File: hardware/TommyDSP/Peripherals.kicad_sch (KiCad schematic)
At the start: 36 parts, among them J501 USB_C_Receptacle_USB2.0_16P, J502 PJ-307, J503 XH-2.50mm Horizontal, J504 PJ-307, J505 Conn_01x06_Pin, J506 PJ-307, J507 XH-2.50mm Horizontal, J508 Conn_01x06_Pin, J509 Conn_01x03_Pin, J510 PJ-307, J511 Micro_SD_Card_Det1, SW501 RotaryEncoder_Switch_MP

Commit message: hardware: finalize PCB design
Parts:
- removed J502, J504, J506, J510: PJ-307, Project:Jack_3.5mm_CUI_SJ1-3525N_Horizontal, symbol Connector_Audio:AudioJack3_Ground_SwitchTR
- added C509: 100n, Capacitor_SMD:C_0603_1608Metric, symbol Device:C
- added G501: qwiic_Logo, SparkFun-Qwiic:qwiic_5.5mm, symbol SparkFun-Qwiic:qwiic_Logo
- added J502, J504, J506, J510: AudioJack3_SwitchTR, Project:Jack_3.5mm_CUI_SJ1-3525N_Horizontal, symbol Connector_Audio:AudioJack3_SwitchTR
- added J512: Qwiic, Connector_JST:JST_SH_SM04B-SRSS-TB_1x04-1MP_P1.00mm_Horizontal, symbol Connector_Generic_MountingPin:Conn_01x04_MountingPin
- J505: value Conn_01x06_Pin -> EXT.IN
- J508: value Conn_01x06_Pin -> EXT.OUT
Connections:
- net +3V3: now also C509.1, J512.2 (Pin_2)
- net GND: now also C509.2, J502.S, J504.S, J506.S, J510.S, J512.1 (Pin_1), J512.MP (MountPin)
- net HPOUT_L: now also J506.T, J506.TN
- net HPOUT_R: now also J506.R, J506.RN
- net LINEIN_L: now also J504.T, J504.TN
- net LINEIN_R: now also J504.R, J504.RN
- net LINEOUT_L: now also J510.T, J510.TN
- net LINEOUT_R: now also J510.R, J510.RN
- net MIC_L: now also J502.T, J502.TN
- net MIC_R: now also J502.R, J502.RN
- new net I2C_SCL: J512.4 (Pin_4)
- new net I2C_SDA: J512.3 (Pin_3)

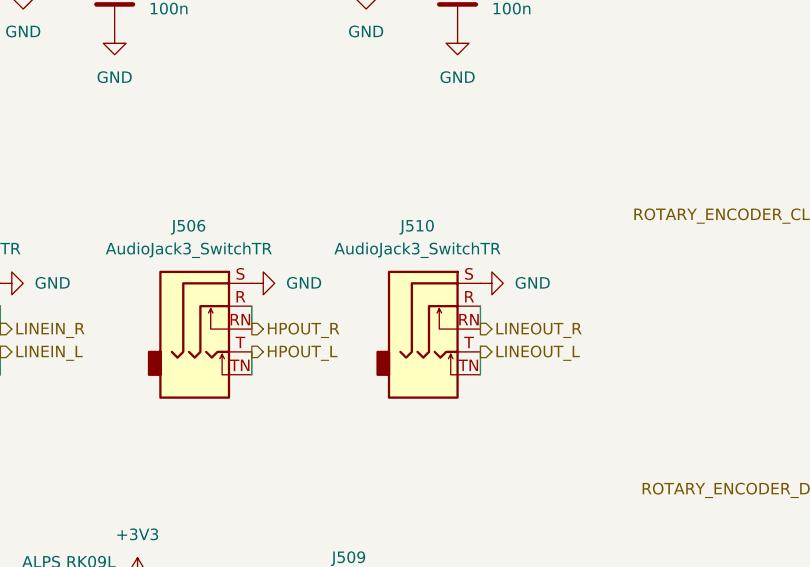
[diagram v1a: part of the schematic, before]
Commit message: hardware: add compatibility for WM8988 CODEC
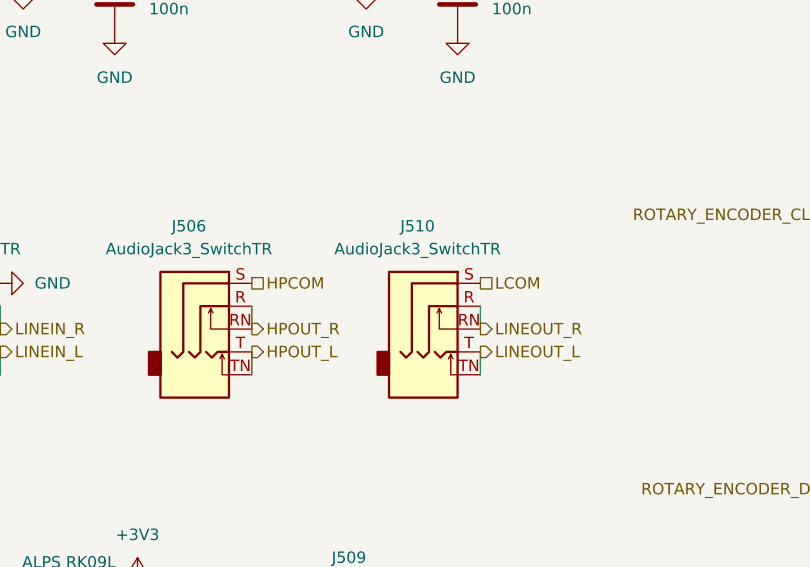
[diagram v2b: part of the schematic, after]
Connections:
- net GND: no longer J506.S, J510.S
- new net HPCOM: J506.S
- new net LCOM: J510.S
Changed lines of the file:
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@@
 		)
 	)
+	(hierarchical_label "HPCOM"
+		(shape passive)
+		(at 93.98 121.92 0)
+		(effects
+			(font
+				(size 1.27 1.27)
+			)
+			(justify left)
+		)
+	)
 	(hierarchical_label "ROTARY_ENCODER_DT"
 		(shape output)
@@
 		)
 	)
+	(hierarchical_label "LCOM"
+		(shape passive)
+		(at 119.38 121.92 0)
+		(effects
+			(font
+				(size 1.27 1.27)
+			)
+			(justify left)
+		)
+	)
 	(hierarchical_label "LCD_BL"
 		(shape input)
@@
 	(symbol
 		(lib_id "power:GND")
-		(at 93.98 121.92 90)
-		(unit 1)
-		(exclude_from_sim no)
-		(in_bom yes)
-		(on_board yes)
-		(dnp no)
-		(fields_autoplaced yes)
-		(property "Reference" "#PWR0524"
-			(at 100.33 121.92 0)
-			(effects
-				(font
-					(size 1.27 1.27)
-				)
-				(hide yes)
-			)
-		)
-		(property "Value" "GND"
-			(at 97.79 121.9199 90)
-			(effects
-				(font
-					(size 1.27 1.27)
-				)
-				(justify right)
-			)
-		)
-		(property "Footprint" ""
-			(at 93.98 121.92 0)
-			(effects
-				(font
-					(size 1.27 1.27)
-				)
-				(hide yes)
-			)
-		)
-		(property "Datasheet" ""
-			(at 93.98 121.92 0)
-			(effects
-				(font
-					(size 1.27 1.27)
-				)
-				(hide yes)
-			)
-		)
-		(property "Description" "Power symbol creates a global label with name \"GND\" , ground"
-			(at 93.98 121.92 0)
-			(effects
-				(font
-					(size 1.27 1.27)
-				)
-				(hide yes)
-			)
-		)
-		(pin "1"
-		)
-		(instances
-			(project "TommyDSP"
-				(path "/8e0e2dd5-fa84-4cc4-affc-8a947fbe8a29/0bcb7ca8-b020-48a0-860c-aef49da61744"
-					(reference "#PWR0524")
-					(unit 1)
-				)
-			)
-		)
-	)
-	(symbol
-		(lib_id "power:GND")
 		(at 215.9 139.7 270)
 		(unit 1)
@@
 					(unit 1)
 				)
-			)
-		)
-	)
-	(symbol
-		(lib_id "power:GND")
-		(at 119.38 121.92 90)
-		(unit 1)
-		(exclude_from_sim no)
-		(in_bom yes)
-		(on_board yes)
-		(dnp no)
-		(fields_autoplaced yes)
-		(property "Reference" "#PWR0535"
-			(at 125.73 121.92 0)
-			(effects
-				(font
-					(size 1.27 1.27)
-				)
-				(hide yes)
-			)
-		)
-		(property "Value" "GND"
-			(at 123.19 121.9199 90)
-			(effects
-				(font
-					(size 1.27 1.27)
-				)
-				(justify right)
-			)
-		)
-		(property "Footprint" ""
-			(at 119.38 121.92 0)
-			(effects
-				(font
-					(size 1.27 1.27)
-				)
-				(hide yes)
-			)
-		)
-		(property "Datasheet" ""
-			(at 119.38 121.92 0)
-			(effects
-				(font
-					(size 1.27 1.27)
-				)
-				(hide yes)
-			)
-		)
-		(property "Description" "Power symbol creates a global label with name \"GND\" , ground"
-			(at 119.38 121.92 0)
-			(effects
-				(font
-					(size 1.27 1.27)
-				)
-				(hide yes)
-			)
-		)
-		(pin "1"
-		)
-		(instances
-			(project "TommyDSP"
-				(path "/8e0e2dd5-fa84-4cc4-affc-8a947fbe8a29/0bcb7ca8-b020-48a0-860c-aef49da61744"
-					(reference "#PWR0535")
-					(unit 1)
-				)
